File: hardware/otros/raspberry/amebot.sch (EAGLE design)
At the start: 7 parts, among them IC1 L293DB

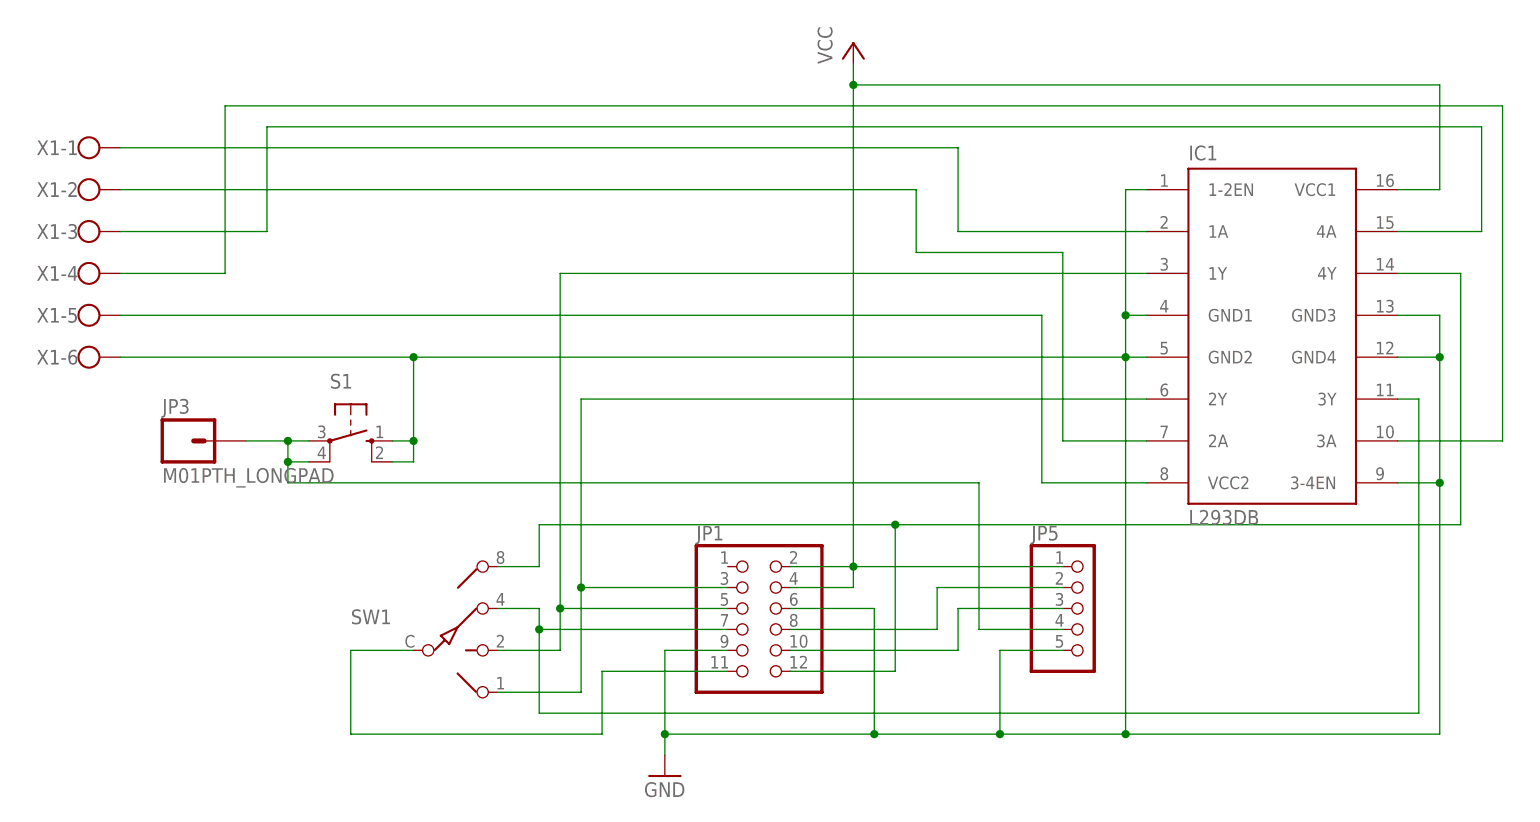
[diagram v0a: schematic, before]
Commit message: 
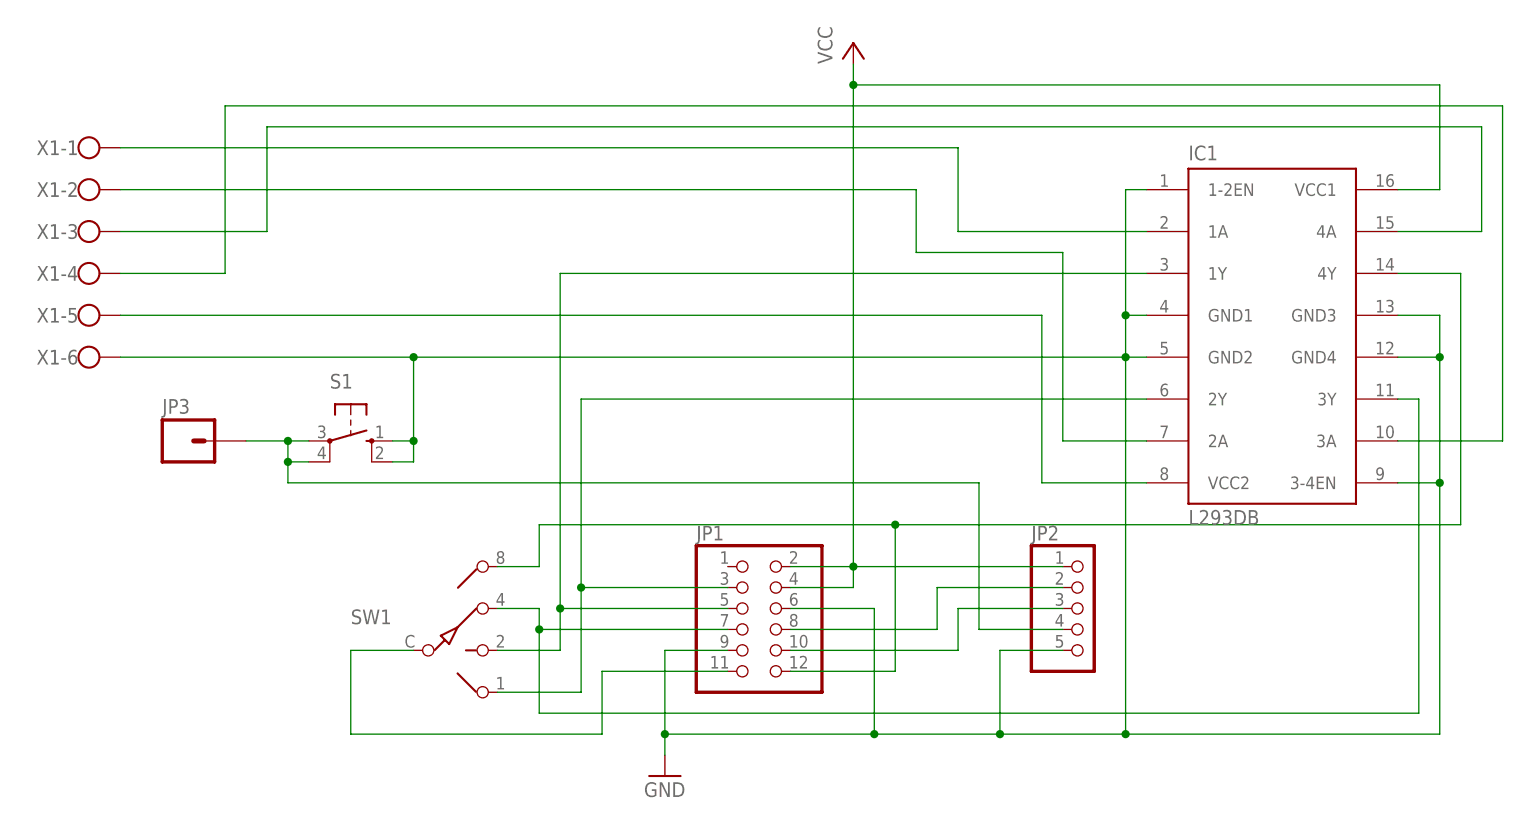
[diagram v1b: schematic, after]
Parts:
- renumbered JP5 to JP2
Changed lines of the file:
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@@
 <grid distance="0.1" unitdist="inch" unit="inch" style="lines" multiple="1" display="no" altdistance="0.01" altunitdist="inch" altunit="inch"/>
 <layers>
-<layer number="1" name="Top" color="4" fill="1" visible="yes" active="no"/>
-<layer number="2" name="Route2" color="1" fill="3" visible="yes" active="no"/>
-<layer number="3" name="Route3" color="4" fill="3" visible="yes" active="no"/>
-<layer number="4" name="Route4" color="1" fill="4" visible="yes" active="no"/>
-<layer number="5" name="Route5" color="4" fill="4" visible="yes" active="no"/>
-<layer number="6" name="Route6" color="1" fill="8" visible="yes" active="no"/>
-<layer number="7" name="Route7" color="4" fill="8" visible="yes" active="no"/>
-<layer number="8" name="Route8" color="1" fill="2" visible="yes" active="no"/>
-<layer number="9" name="Route9" color="4" fill="2" visible="yes" active="no"/>
-<layer number="10" name="Route10" color="1" fill="7" visible="yes" active="no"/>
-<layer number="11" name="Route11" color="4" fill="7" visible="yes" active="no"/>
-<layer number="12" name="Route12" color="1" fill="5" visible="yes" active="no"/>
-<layer number="13" name="Route13" color="4" fill="5" visible="yes" active="no"/>
-<layer number="14" name="Route14" color="1" fill="6" visible="yes" active="no"/>
-<layer number="15" name="Route15" color="4" fill="6" visible="yes" active="no"/>
-<layer number="16" name="Bottom" color="1" fill="1" visible="yes" active="no"/>
-<layer number="17" name="Pads" color="2" fill="1" visible="yes" active="no"/>
-<layer number="18" name="Vias" color="2" fill="1" visible="yes" active="no"/>
-<layer number="19" name="Unrouted" color="6" fill="1" visible="yes" active="no"/>
-<layer number="20" name="Dimension" color="15" fill="1" visible="yes" active="no"/>
-<layer number="21" name="tPlace" color="7" fill="1" visible="yes" active="no"/>
-<layer number="22" name="bPlace" color="7" fill="1" visible="yes" active="no"/>
-<layer number="23" name="tOrigins" color="15" fill="1" visible="yes" active="no"/>
-<layer number="24" name="bOrigins" color="15" fill="1" visible="yes" active="no"/>
-<layer number="25" name="tNames" color="7" fill="1" visible="yes" active="no"/>
-<layer number="26" name="bNames" color="7" fill="1" visible="yes" active="no"/>
-<layer number="27" name="tValues" color="7" fill="1" visible="yes" active="no"/>
-<layer number="28" name="bValues" color="7" fill="1" visible="yes" active="no"/>
+<layer number="1" name="Top" color="4" fill="1" visible="no" active="no"/>
+<layer number="2" name="Route2" color="1" fill="3" visible="no" active="no"/>
+<layer number="3" name="Route3" color="4" fill="3" visible="no" active="no"/>
+<layer number="4" name="Route4" color="1" fill="4" visible="no" active="no"/>
+<layer number="5" name="Route5" color="4" fill="4" visible="no" active="no"/>
+<layer number="6" name="Route6" color="1" fill="8" visible="no" active="no"/>
+<layer number="7" name="Route7" color="4" fill="8" visible="no" active="no"/>
+<layer number="8" name="Route8" color="1" fill="2" visible="no" active="no"/>
+<layer number="9" name="Route9" color="4" fill="2" visible="no" active="no"/>
+<layer number="10" name="Route10" color="1" fill="7" visible="no" active="no"/>
+<layer number="11" name="Route11" color="4" fill="7" visible="no" active="no"/>
+<layer number="12" name="Route12" color="1" fill="5" visible="no" active="no"/>
+<layer number="13" name="Route13" color="4" fill="5" visible="no" active="no"/>
+<layer number="14" name="Route14" color="1" fill="6" visible="no" active="no"/>
+<layer number="15" name="Route15" color="4" fill="6" visible="no" active="no"/>
+<layer number="16" name="Bottom" color="1" fill="1" visible="no" active="no"/>
+<layer number="17" name="Pads" color="2" fill="1" visible="no" active="no"/>
+<layer number="18" name="Vias" color="2" fill="1" visible="no" active="no"/>
+<layer number="19" name="Unrouted" color="6" fill="1" visible="no" active="no"/>
+<layer number="20" name="Dimension" color="15" fill="1" visible="no" active="no"/>
+<layer number="21" name="tPlace" color="7" fill="1" visible="no" active="no"/>
+<layer number="22" name="bPlace" color="7" fill="1" visible="no" active="no"/>
+<layer number="23" name="tOrigins" color="15" fill="1" visible="no" active="no"/>
+<layer number="24" name="bOrigins" color="15" fill="1" visible="no" active="no"/>
+<layer number="25" name="tNames" color="7" fill="1" visible="no" active="no"/>
+<layer number="26" name="bNames" color="7" fill="1" visible="no" active="no"/>
+<layer number="27" name="tValues" color="7" fill="1" visible="no" active="no"/>
+<layer number="28" name="bValues" color="7" fill="1" visible="no" active="no"/>
 <layer number="29" name="tStop" color="7" fill="3" visible="no" active="no"/>
 <layer number="30" name="bStop" color="7" fill="6" visible="no" active="no"/>
@@
 <layer number="35" name="tGlue" color="7" fill="4" visible="no" active="no"/>
 <layer number="36" name="bGlue" color="7" fill="5" visible="no" active="no"/>
-<layer number="37" name="tTest" color="7" fill="1" visible="yes" active="no"/>
-<layer number="38" name="bTest" color="7" fill="1" visible="yes" active="no"/>
+<layer number="37" name="tTest" color="7" fill="1" visible="no" active="no"/>
+<layer number="38" name="bTest" color="7" fill="1" visible="no" active="no"/>
 <layer number="39" name="tKeepout" color="4" fill="11" visible="no" active="no"/>
 <layer number="40" name="bKeepout" color="1" fill="11" visible="no" active="no"/>
@@
 <layer number="44" name="Drills" color="7" fill="1" visible="no" active="no"/>
 <layer number="45" name="Holes" color="7" fill="1" visible="no" active="no"/>
-<layer number="46" name="Milling" color="3" fill="1" visible="yes" active="no"/>
-<layer number="47" name="Measures" color="7" fill="1" visible="yes" active="no"/>
-<layer number="48" name="Document" color="7" fill="1" visible="yes" active="no"/>
-<layer number="49" name="Reference" color="7" fill="1" visible="yes" active="no"/>
-<layer number="50" name="dxf" color="7" fill="1" visible="yes" active="no"/>
-<layer number="51" name="tDocu" color="7" fill="1" visible="yes" active="no"/>
-<layer number="52" name="bDocu" color="7" fill="1" visible="yes" active="no"/>
-<layer number="53" name="tGND_GNDA" color="7" fill="9" visible="yes" active="no"/>
-<layer number="54" name="bGND_GNDA" color="1" fill="9" visible="yes" active="no"/>
-<layer number="56" name="wert" color="7" fill="1" visible="yes" active="no"/>
-<layer number="57" name="tCAD" color="7" fill="1" visible="yes" active="no"/>
+<layer number="46" name="Milling" color="3" fill="1" visible="no" active="no"/>
+<layer number="47" name="Measures" color="7" fill="1" visible="no" active="no"/>
+<layer number="48" name="Document" color="7" fill="1" visible="no" active="no"/>
+<layer number="49" name="Reference" color="7" fill="1" visible="no" active="no"/>
+<layer number="50" name="dxf" color="7" fill="1" visible="no" active="no"/>
+<layer number="51" name="tDocu" color="7" fill="1" visible="no" active="no"/>
+<layer number="52" name="bDocu" color="7" fill="1" visible="no" active="no"/>
+<layer number="53" name="tGND_GNDA" color="7" fill="9" visible="no" active="no"/>
+<layer number="54" name="bGND_GNDA" color="1" fill="9" visible="no" active="no"/>
+<layer number="56" name="wert" color="7" fill="1" visible="no" active="no"/>
+<layer number="57" name="tCAD" color="7" fill="1" visible="no" active="no"/>
 <layer number="91" name="Nets" color="2" fill="1" visible="yes" active="yes"/>
 <layer number="92" name="Busses" color="1" fill="1" visible="yes" active="yes"/>
@@
 <part name="GND1" library="supply1" deviceset="GND" device=""/>
 <part name="P+1" library="supply1" deviceset="VCC" device=""/>
-<part name="JP3" library="SparkFun-Connectors" deviceset="M01" device="PTH_LONGPAD"/>
+<part name="JP3" library="SparkFun-Connectors" deviceset="M01" device="PTH_LONGPAD" value=""/>
 <part name="S1" library="switch-omron" deviceset="10-XX" device=""/>
-<part name="JP5" library="pinhead" deviceset="PINHD-1X5" device=""/>
+<part name="JP2" library="pinhead" deviceset="PINHD-1X5" device=""/>
 </parts>
 <sheets>
@@
 <instance part="JP3" gate="G$1" x="-7.62" y="55.88"/>
 <instance part="S1" gate="1" x="12.7" y="55.88" rot="R270"/>
-<instance part="JP5" gate="A" x="101.6" y="35.56"/>
+<instance part="JP2" gate="A" x="101.6" y="35.56"/>
 </instances>
 <busses>
@@
 <wire x1="91.44" y1="30.48" x2="91.44" y2="20.32" width="0.1524" layer="91"/>
 <junction x="91.44" y="20.32"/>
-<pinref part="JP5" gate="A" pin="5"/>
+<pinref part="JP2" gate="A" pin="5"/>
 <wire x1="91.44" y1="30.48" x2="99.06" y2="30.48" width="0.1524" layer="91"/>
 </segment>
@@
 <wire x1="73.66" y1="99.06" x2="73.66" y2="101.6" width="0.1524" layer="91"/>
 <junction x="73.66" y="99.06"/>
-<pinref part="JP5" gate="A" pin="1"/>
+<pinref part="JP2" gate="A" pin="1"/>
 <wire x1="99.06" y1="40.64" x2="73.66" y2="40.64" width="0.1524" layer="91"/>
 </segment>
@@
 <wire x1="5.08" y1="50.8" x2="5.08" y2="53.34" width="0.1524" layer="91"/>
 <junction x="5.08" y="53.34"/>
-<pinref part="JP5" gate="A" pin="4"/>
+<pinref part="JP2" gate="A" pin="4"/>
 <wire x1="88.9" y1="33.02" x2="99.06" y2="33.02" width="0.1524" layer="91"/>
 </segment>
@@
 <wire x1="66.04" y1="33.02" x2="83.82" y2="33.02" width="0.1524" layer="91"/>
 <wire x1="83.82" y1="33.02" x2="83.82" y2="38.1" width="0.1524" layer="91"/>
-<pinref part="JP5" gate="A" pin="2"/>
+<pinref part="JP2" gate="A" pin="2"/>
 <wire x1="83.82" y1="38.1" x2="99.06" y2="38.1" width="0.1524" layer="91"/>
 </segment>
@@
 <wire x1="66.04" y1="30.48" x2="86.36" y2="30.48" width="0.1524" layer="91"/>
 <wire x1="86.36" y1="30.48" x2="86.36" y2="35.56" width="0.1524" layer="91"/>
-<pinref part="JP5" gate="A" pin="3"/>
+<pinref part="JP2" gate="A" pin="3"/>
 <wire x1="86.36" y1="35.56" x2="99.06" y2="35.56" width="0.1524" layer="91"/>
 </segment>

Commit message: Error en los enables
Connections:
- net GND: no longer IC1.1-2EN, IC1.3-4EN
- net VCC: now also IC1.1-2EN, IC1.3-4EN
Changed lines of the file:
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@@
 <pinref part="IC1" gate="G$1" pin="GND4"/>
 <wire x1="144.78" y1="66.04" x2="139.7" y2="66.04" width="0.1524" layer="91"/>
-<wire x1="144.78" y1="66.04" x2="144.78" y2="50.8" width="0.1524" layer="91"/>
 <junction x="144.78" y="66.04"/>
 <pinref part="JP1" gate="A" pin="6"/>
-<wire x1="144.78" y1="50.8" x2="144.78" y2="20.32" width="0.1524" layer="91"/>
+<wire x1="144.78" y1="66.04" x2="144.78" y2="20.32" width="0.1524" layer="91"/>
 <pinref part="JP1" gate="A" pin="9"/>
 <wire x1="76.2" y1="35.56" x2="66.04" y2="35.56" width="0.1524" layer="91"/>
@@
 <wire x1="106.68" y1="66.04" x2="106.68" y2="20.32" width="0.1524" layer="91"/>
 <junction x="106.68" y="20.32"/>
-<pinref part="IC1" gate="G$1" pin="1-2EN"/>
-<wire x1="109.22" y1="86.36" x2="106.68" y2="86.36" width="0.1524" layer="91"/>
-<wire x1="106.68" y1="86.36" x2="106.68" y2="71.12" width="0.1524" layer="91"/>
-<junction x="106.68" y="71.12"/>
-<pinref part="IC1" gate="G$1" pin="3-4EN"/>
-<wire x1="139.7" y1="50.8" x2="144.78" y2="50.8" width="0.1524" layer="91"/>
-<junction x="144.78" y="50.8"/>
 <pinref part="S1" gate="1" pin="S1"/>
 <wire x1="17.78" y1="53.34" x2="20.32" y2="53.34" width="0.1524" layer="91"/>
@@
 <wire x1="139.7" y1="86.36" x2="144.78" y2="86.36" width="0.1524" layer="91"/>
 <wire x1="144.78" y1="86.36" x2="144.78" y2="99.06" width="0.1524" layer="91"/>
-<wire x1="144.78" y1="99.06" x2="73.66" y2="99.06" width="0.1524" layer="91"/>
+<wire x1="144.78" y1="99.06" x2="106.68" y2="99.06" width="0.1524" layer="91"/>
+<wire x1="106.68" y1="99.06" x2="73.66" y2="99.06" width="0.1524" layer="91"/>
 <wire x1="73.66" y1="99.06" x2="73.66" y2="40.64" width="0.1524" layer="91"/>
 <junction x="73.66" y="40.64"/>
@@
 <pinref part="JP2" gate="A" pin="1"/>
 <wire x1="99.06" y1="40.64" x2="73.66" y2="40.64" width="0.1524" layer="91"/>
+<pinref part="IC1" gate="G$1" pin="1-2EN"/>
+<wire x1="109.22" y1="86.36" x2="106.68" y2="86.36" width="0.1524" layer="91"/>
+<wire x1="106.68" y1="86.36" x2="106.68" y2="99.06" width="0.1524" layer="91"/>
+<junction x="106.68" y="99.06"/>
+<pinref part="IC1" gate="G$1" pin="3-4EN"/>
+<wire x1="139.7" y1="50.8" x2="154.94" y2="50.8" width="0.1524" layer="91"/>
+<wire x1="154.94" y1="50.8" x2="154.94" y2="99.06" width="0.1524" layer="91"/>
+<wire x1="154.94" y1="99.06" x2="144.78" y2="99.06" width="0.1524" layer="91"/>
+<junction x="144.78" y="99.06"/>
 </segment>
 </net>
